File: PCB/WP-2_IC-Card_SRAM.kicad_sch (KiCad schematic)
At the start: 19 parts, among them J1 SMS-138-01-G-S, SW1 CUS-14TB, U1 AS6C4008

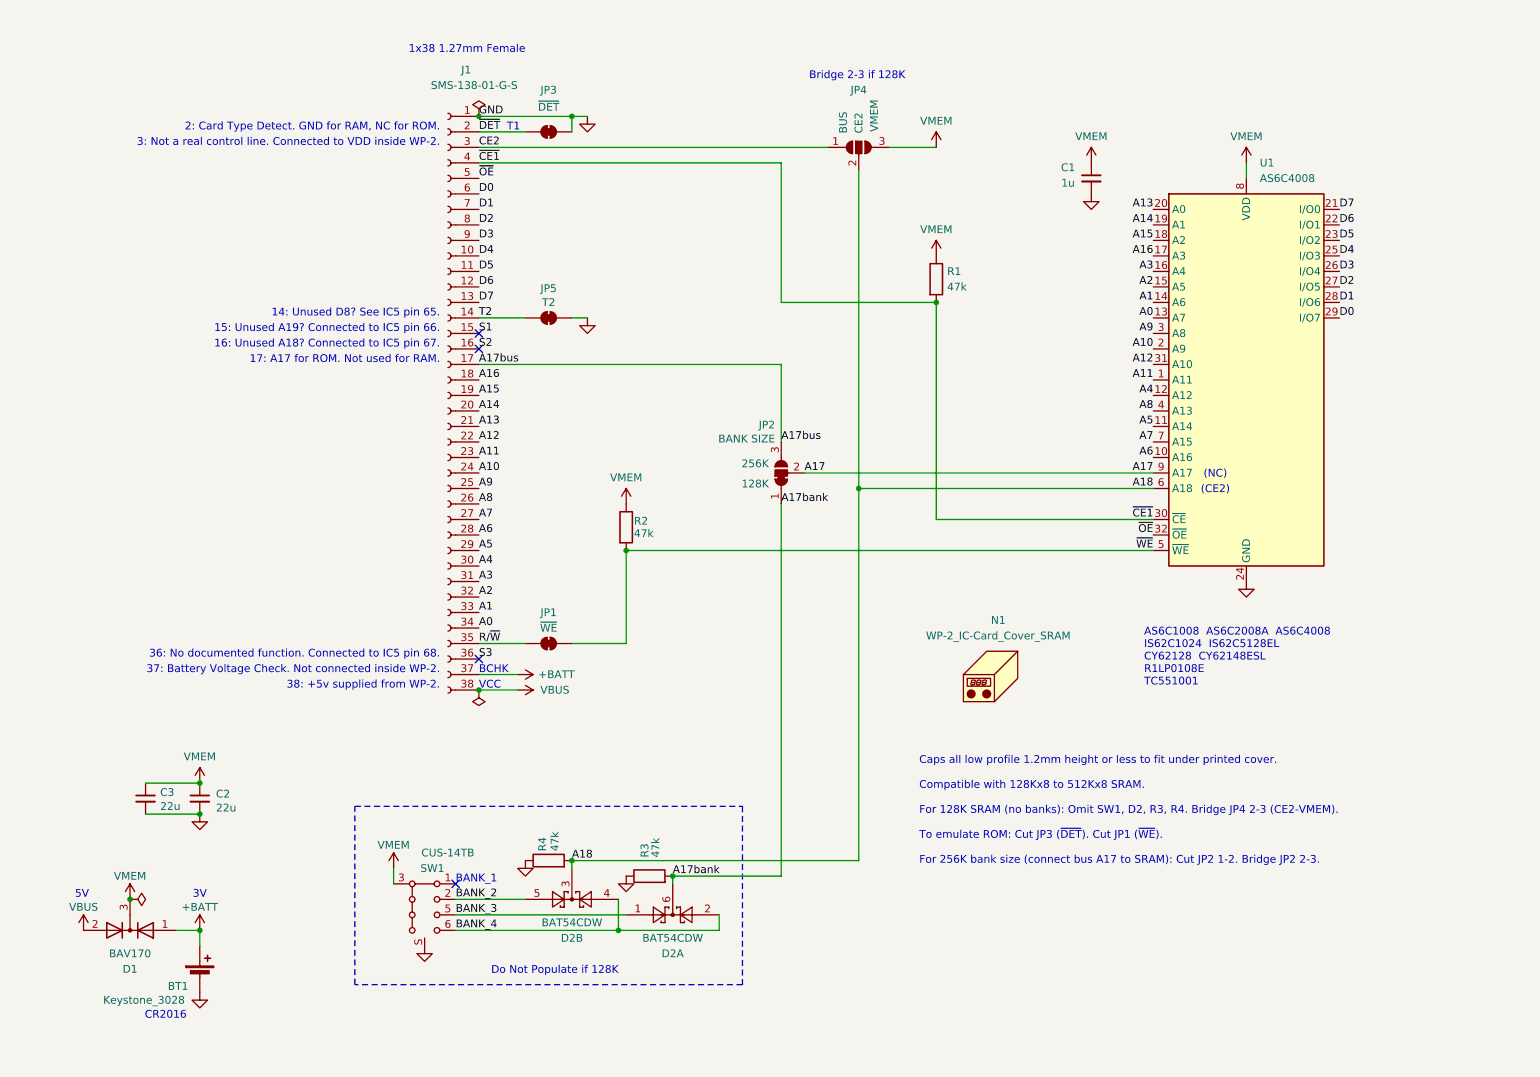
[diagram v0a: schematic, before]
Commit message: refactor cover scad more, cover models makefile, adjust new sram switch & batt positions
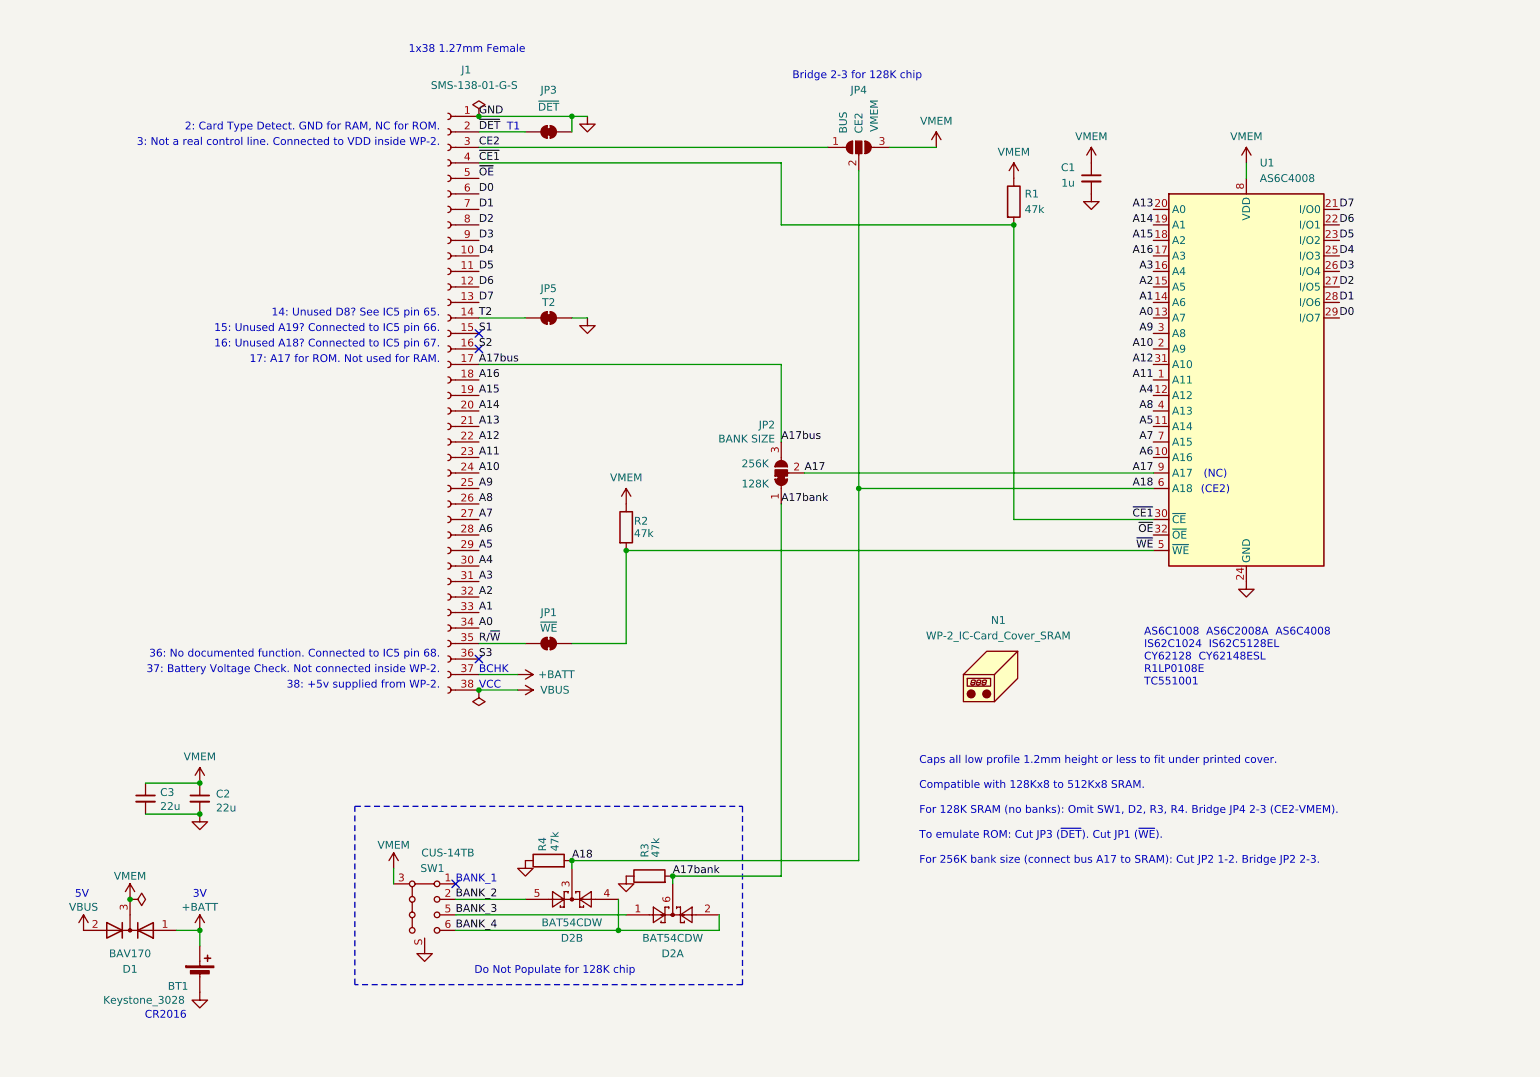
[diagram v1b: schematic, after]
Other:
- note added: "Bridge 2-3 for 128K chip"
- note added: "Do Not Populate for 128K chip"
- note removed: "Bridge 2-3 if 128K"
- note removed: "Do Not Populate if 128K"
- moved on the sheet: R1
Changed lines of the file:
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@@
 	(title_block
 		(title "WP-2_IC-Card_SRAM")
-		(date "2025-04-22")
+		(date "2025-04-25")
 		(rev "020")
 		(company "Brian K. White - b.kenyon.w@gmail.com")
@@
 	)
 	(junction
-		(at 165.1 76.2)
-		(diameter 0)
-		(color 0 0 0 0)
-	)
-	(junction
 		(at 44.45 154.94)
 		(diameter 0)
@@
 	)
 	(junction
+		(at 177.8 63.5)
+		(diameter 0)
+		(color 0 0 0 0)
+	)
+	(junction
 		(at 121.92 170.18)
 		(diameter 0)
@@
 	(wire
 		(pts
-			(xy 139.7 76.2) (xy 165.1 76.2)
+			(xy 139.7 63.5) (xy 177.8 63.5)
 		)
 		(stroke
@@
 	(wire
 		(pts
-			(xy 139.7 76.2) (xy 139.7 53.34)
+			(xy 139.7 63.5) (xy 139.7 53.34)
 		)
 		(stroke
@@
 	(wire
 		(pts
-			(xy 200.66 111.76) (xy 165.1 111.76)
+			(xy 200.66 111.76) (xy 177.8 111.76)
 		)
 		(stroke
@@
 	(wire
 		(pts
-			(xy 165.1 76.2) (xy 165.1 111.76)
-		)
-		(stroke
-			(width 0)
-			(type default)
-		)
-	)
-	(wire
-		(pts
 			(xy 113.03 179.07) (xy 129.54 179.07)
 		)
@@
 		(pts
 			(xy 105.41 167.64) (xy 105.41 168.91)
+		)
+		(stroke
+			(width 0)
+			(type default)
+		)
+	)
+	(wire
+		(pts
+			(xy 177.8 63.5) (xy 177.8 111.76)
 		)
 		(stroke
@@
 		)
 	)
-	(text "Bridge 2-3 if 128K\n"
+	(text "Bridge 2-3 for 128K chip\n"
 		(exclude_from_sim no)
 		(at 152.146 39.116 0)
@@
 		)
 	)
-	(text "Do Not Populate if 128K"
+	(text "Do Not Populate for 128K chip"
 		(exclude_from_sim no)
 		(at 102.616 186.436 0)
@@
 	(symbol
 		(lib_id "000_LOCAL:R")
-		(at 165.1 72.39 0)
+		(at 177.8 59.69 0)
 		(unit 1)
 		(exclude_from_sim no)
@@
 		(dnp no)
 		(property "Reference" "R1"
-			(at 166.878 71.12 0)
+			(at 179.578 58.42 0)
 			(effects
 				(font
@@
 		)
 		(property "Value" "47k"
-			(at 166.878 73.66 0)
+			(at 179.578 60.96 0)
 			(effects
 				(font
@@
 		)
 		(property "Footprint" "000_LOCAL:R_0805"
-			(at 165.1 72.39 0)
+			(at 177.8 59.69 0)
 			(effects
 				(font
@@
 		)
 		(property "Datasheet" "datasheets/sei-rmcf_rmcp.pdf"
-			(at 165.1 72.39 0)
+			(at 177.8 59.69 0)
 			(effects
 				(font
@@
 		)
 		(property "Description" "RES 47K OHM 1% 1/8W 0805"
-			(at 165.1 72.39 0)
+			(at 177.8 59.69 0)
 			(effects
 				(font
@@
 		)
 		(property "MPN" "RMCF0805FT47K0"
-			(at 165.1 72.39 0)
+			(at 177.8 59.69 0)
 			(effects
 				(font
@@
 	(symbol
 		(lib_id "power:VMEM")
-		(at 165.1 68.58 0)
+		(at 177.8 55.88 0)
 		(unit 1)
 		(exclude_from_sim no)
@@
 		(dnp no)
 		(property "Reference" "#PWR016"
-			(at 165.1 72.39 0)
+			(at 177.8 59.69 0)
 			(effects
 				(font
@@
 		)
 		(property "Value" "VMEM"
-			(at 165.1 64.262 0)
+			(at 177.8 51.562 0)
 			(effects
 				(font
@@
 		)
 		(property "Footprint" ""
-			(at 165.1 68.58 0)
+			(at 177.8 55.88 0)
 			(effects
 				(font
@@
 		)
 		(property "Datasheet" ""
-			(at 165.1 68.58 0)
+			(at 177.8 55.88 0)
 			(effects
 				(font
@@
 		)
 		(property "Description" ""
-			(at 165.1 68.58 0)
-			(effects
-				(font
+			(at 177.8 55.88 0)
+			(effects
+				(font

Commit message: SRAM battery life, bank sw use vbus
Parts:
- D2: value BAT54CDW -> BAV70S; symbol 000_LOCAL:BAT54CDW -> 000_LOCAL:BAV70S; MPN BAT54CDW-7-F -> BAV70S,135
- JP2: L12 128K -> (none); L23 256K -> (none); Label_1-2 (none) -> 128K; Label_2-3 (none) -> 256K
- JP4: L12 BUS -> (none); L23 VMEM -> (none); Label_1-2 (none) -> BUS; Label_2-3 (none) -> VMEM; now left out of the parts list
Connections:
- net VBUS: now also SW1.3 (C), SW1.4 (C)
- net VMEM: no longer SW1.3 (C), SW1.4 (C)
- net A18 renamed A18_CE2
- net CE2 renamed CE2bus
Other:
- note added: "128K or 256K: join BUS-CE2 512K: both open"
- note added: "CR2012 (can hold CR2016 if you bend the tabs down slightly before soldering)"
- note added: "Caps all low profile 1.2mm height or less to fit under printed cover. Compatible with 128Kx8 to 512Kx8 SRAM. For 128K SRAM (no banks): Omit SW1, D2, R3, R4. Bridge JP4 1-2 (BUS-CE2). To emulate ROM: Cut JP3 (~{DET}). Cut JP1 (~{WE}). For 256K bank size (connect bus A17 to SRAM): Cut JP2 1-2. Bridge JP2 2-3."
- note removed: "Bridge 2-3 for 128K chip"
- note removed: "CR2016"
- note removed: "Caps all low profile 1.2mm height or less to fit under printed cover. Compatible with 128Kx8 to 512Kx8 SRAM. For 128K SRAM (no banks): Omit SW1, D2, R3, R4. Bridge JP4 2-3 (CE2-VMEM). To emulate ROM: Cut JP3 (~{DET}). Cut JP1 (~{WE}). For 256K bank size (connect bus A17 to SRAM): Cut JP2 1-2. Bridge JP2 2-3."

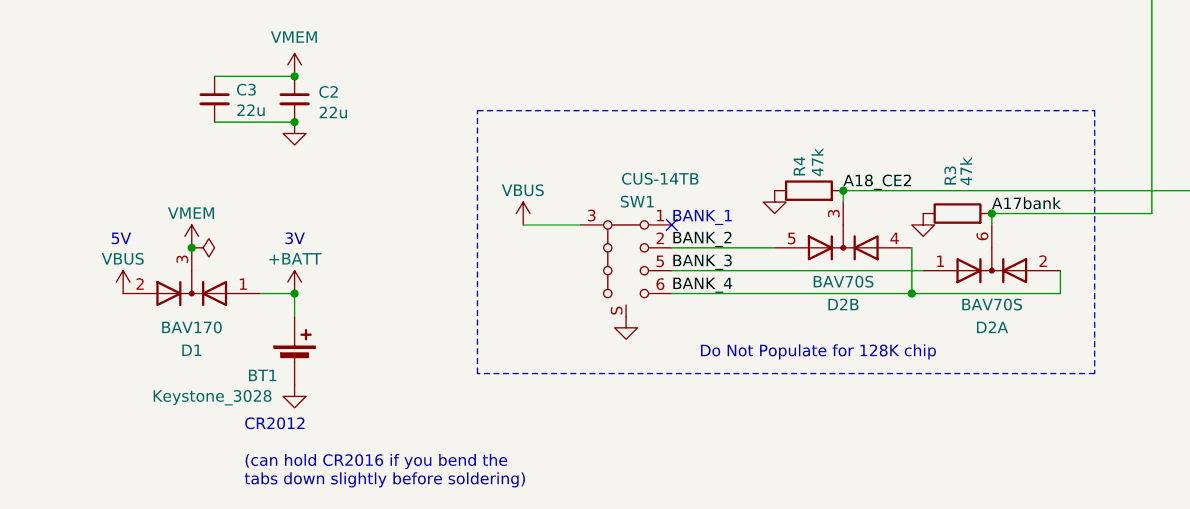
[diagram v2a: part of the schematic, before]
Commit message: SRAM simpler diodes
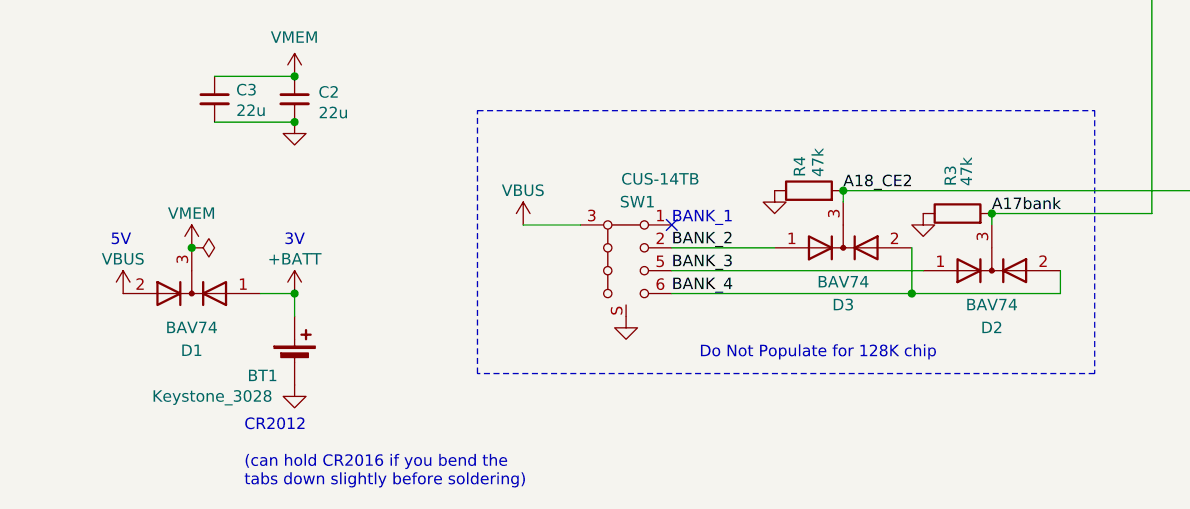
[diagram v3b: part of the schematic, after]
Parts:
- removed D2: BAV70S, 000_LOCAL:TSSOP-6-symmetric, symbol 000_LOCAL:BAV70S
- added D2, D3: BAV74, 000_LOCAL:SOT-23, symbol 000_LOCAL:BAV170
- D1: value BAV170 -> BAV74; MPN BAV170-7-F -> BAV74-TP
- U1: MPN AS6C4008-55TIN -> AS6C4008-55STIN
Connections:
- net A17bank: now also D2.3 (K)
- net A18_CE2: now also D3.3 (K)
- net BANK_2: now also D3.1 (A)
- net BANK_3: now also D2.1 (A)
- net BANK_4: now also D2.2 (A), D3.2 (A)
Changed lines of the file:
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@@
 	(title_block
 		(title "WP-2_IC-Card_SRAM")
-		(date "2025-09-28")
-		(rev "021")
+		(date "2025-09-29")
+		(rev "022")
 		(company "Brian K. White - b.kenyon.w@gmail.com")
 	)
@@
 	)
 	(symbol
-		(lib_name "BAV70S_1")
-		(lib_id "000_LOCAL:BAV70S")
-		(at 121.92 176.53 0)
-		(mirror x)
-		(unit 1)
-		(exclude_from_sim no)
-		(in_bom yes)
-		(on_board yes)
-		(dnp no)
-		(property "Reference" "D2"
-			(at 121.92 182.88 0)
-			(effects
-				(font
-					(size 1.27 1.27)
-				)
-			)
-		)
-		(property "Value" "BAV70S"
-			(at 121.92 180.34 0)
-			(effects
-				(font
-					(size 1.27 1.27)
-				)
-			)
-		)
-		(property "Footprint" "000_LOCAL:TSSOP-6-symmetric"
-			(at 121.92 176.53 0)
-			(effects
-				(font
-					(size 1.27 1.27)
-				)
-				(hide yes)
-			)
-		)
-		(property "Datasheet" "datasheets/BAV70S.pdf"
-			(at 121.92 176.53 0)
-			(effects
-				(font
-					(size 1.27 1.27)
-				)
-				(hide yes)
-			)
-		)
-		(property "Description" "DIODE ARRAY 2 pair common cathode general purpose 6-TSSOP SOT-363"
-			(at 121.92 176.53 0)
-			(effects
-				(font
-					(size 1.27 1.27)
-				)
-				(hide yes)
-			)
-		)
-		(property "MPN" "BAV70S,135"
-			(at 121.92 176.53 0)
-			(effects
-				(font
-					(size 1.27 1.27)
-				)
-				(hide yes)
-			)
-		)
-		(pin "1"
-		)
-		(pin "2"
-		)
-		(pin "4"
-		)
-		(pin "6"
-		)
-		(pin "5"
-		)
-		(pin "3"
-		)
-		(instances
-			(project "WP-2_IC-Card_SRAM"
-				(path "/61a4a6ea-f14c-4701-87bd-6399392c074d"
-					(reference "D2")
-					(unit 1)
-				)
-			)
-		)
-	)
-	(symbol
 		(lib_id "000_LOCAL:R")
 		(at 118.11 170.18 90)
@@
 	)
 	(symbol
+		(lib_id "000_LOCAL:BAV170")
+		(at 121.92 176.53 0)
+		(mirror x)
+		(unit 1)
+		(exclude_from_sim no)
+		(in_bom yes)
+		(on_board yes)
+		(dnp no)
+		(property "Reference" "D2"
+			(at 121.92 182.88 0)
+			(effects
+				(font
+					(size 1.27 1.27)
+				)
+			)
+		)
+		(property "Value" "BAV74"
+			(at 121.92 180.34 0)
+			(effects
+				(font
+					(size 1.27 1.27)
+				)
+			)
+		)
+		(property "Footprint" "000_LOCAL:SOT-23"
+			(at 121.92 176.53 0)
+			(effects
+				(font
+					(size 1.27 1.27)
+				)
+				(hide yes)
+			)
+		)
+		(property "Datasheet" "datasheets/BAV74.pdf"
+			(at 121.92 176.53 0)
+			(effects
+				(font
+					(size 1.27 1.27)
+				)
+				(hide yes)
+			)
+		)
+		(property "Description" "DIODE ARRAY COMMON CATHODE GP SOT23-3"
+			(at 121.92 176.53 0)
+			(effects
+				(font
+					(size 1.27 1.27)
+				)
+				(hide yes)
+			)
+		)
+		(property "MPN" "BAV74-TP"
+			(at 121.92 176.53 0)
+			(effects
+				(font
+					(size 1.27 1.27)
+				)
+				(hide yes)
+			)
+		)
+		(pin "1"
+		)
+		(pin "2"
+		)
+		(pin "3"
+		)
+		(instances
+			(project "WP-2_IC-Card_SRAM"
+				(path "/61a4a6ea-f14c-4701-87bd-6399392c074d"
+					(reference "D2")
+					(unit 1)
+				)
+			)
+		)
+	)
+	(symbol
 		(lib_id "power:GND")
 		(at 190.5 58.42 0)
@@
 	)
 	(symbol
-		(lib_id "000_LOCAL:BAV70S")
-		(at 105.41 173.99 180)
-		(unit 2)
+		(lib_id "000_LOCAL:BAV170")
+		(at 105.41 173.99 0)
+		(mirror x)
+		(unit 1)
 		(exclude_from_sim no)
 		(in_bom yes)
 		(on_board yes)
 		(dnp no)
-		(property "Reference" "D2"
+		(property "Reference" "D3"
 			(at 105.41 180.34 0)
 			(effects
@@
 			)
 		)
-		(property "Value" "BAV70S"
+		(property "Value" "BAV74"
 			(at 105.41 177.8 0)
 			(effects
@@
 			)
 		)
-		(property "Footprint" "000_LOCAL:TSSOP-6-symmetric"
+		(property "Footprint" "000_LOCAL:SOT-23"
 			(at 105.41 173.99 0)
 			(effects
@@
 			)
 		)
-		(property "Datasheet" "datasheets/BAV70S.pdf"
+		(property "Datasheet" "datasheets/BAV74.pdf"
 			(at 105.41 173.99 0)
 			(effects
@@
 			)
 		)
-		(property "Description" "DIODE ARRAY 2 pair common cathode general purpose 6-TSSOP SOT-363"
+		(property "Description" "DIODE ARRAY COMMON CATHODE GP SOT23-3"
 			(at 105.41 173.99 0)
 			(effects
@@
 			)
 		)
-		(property "MPN" "BAV70S,135"
+		(property "MPN" "BAV74-TP"
 			(at 105.41 173.99 0)
 			(effects
@@
 		(pin "2"
 		)
-		(pin "4"
-		)
-		(pin "6"
-		)
-		(pin "5"
-		)
 		(pin "3"
 		)
@@
 			(project "WP-2_IC-Card_SRAM"
 				(path "/61a4a6ea-f14c-4701-87bd-6399392c074d"
-					(reference "D2")
-					(unit 2)
+					(reference "D3")
+					(unit 1)
 				)
 			)
@@
 			)
 		)
-		(property "MPN" "AS6C4008-55TIN"
+		(property "MPN" "AS6C4008-55STIN"
 			(at 215.9 88.9 0)
 			(effects
@@
 			)
 		)
-		(property "Value" "BAV170"
+		(property "Value" "BAV74"
 			(at 33.02 182.88 0)
 			(effects
@@
 			)
 		)
-		(property "Datasheet" "datasheets/BAV170.pdf"
+		(property "Datasheet" "datasheets/BAV74.pdf"
 			(at 33.02 179.07 0)
 			(effects
@@
 			)
 		)
-		(property "Description" "DIODE ARRAY COMMON CATHODE GP 85V 125MA SOT23-3"
+		(property "Description" "DIODE ARRAY COMMON CATHODE GP SOT23-3"
 			(at 33.02 179.07 0)
 			(effects
@@
 			)
 		)
-		(property "MPN" "BAV170-7-F"
+		(property "MPN" "BAV74-TP"
 			(at 33.02 179.07 0)
 			(effects
